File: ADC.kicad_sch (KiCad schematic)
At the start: 83 parts, among them J1 Conn_01x03_Pin, J2 Screw_Terminal_01x02, J3 Screw_Terminal_01x08, SW1 SW_SPDT, U1 ADS1256IDBR, U12 ADR421ARMZ, U2 MCU-STM32F407VET6_LQFP100_, U3 ADM2483xRW, U4 LM2596S-5, U5 DCP010505BP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

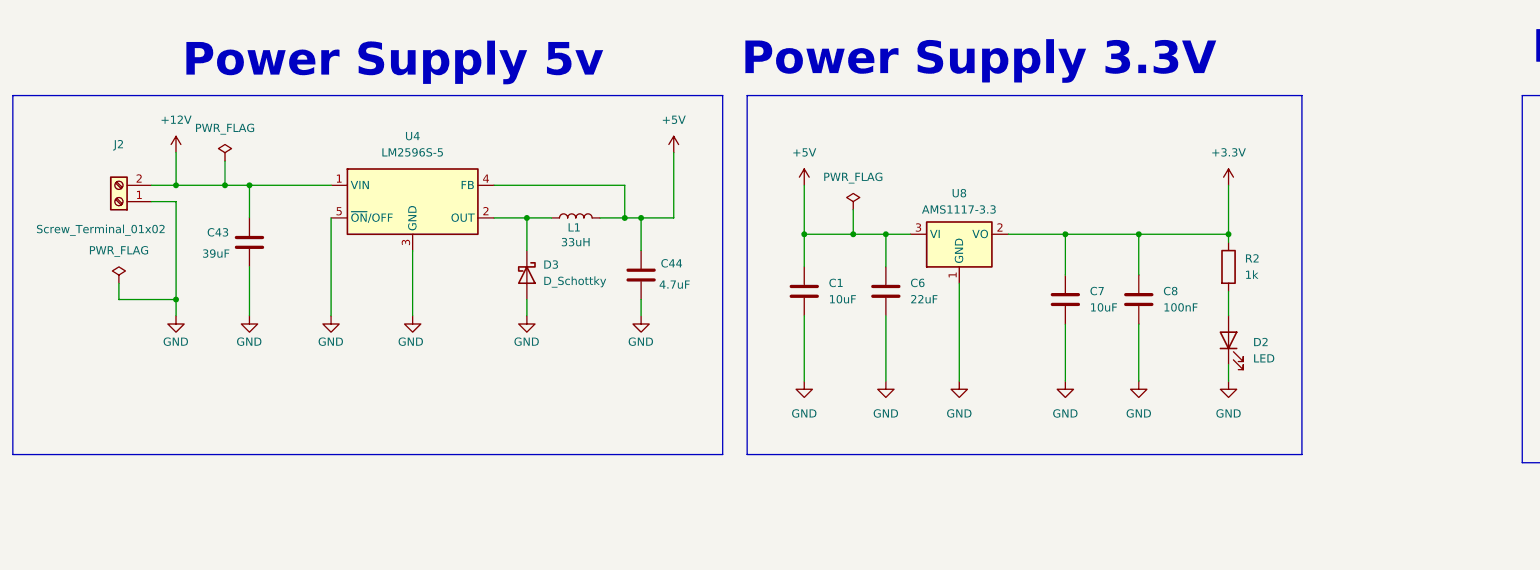
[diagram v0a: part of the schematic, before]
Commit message: Sửa tụ
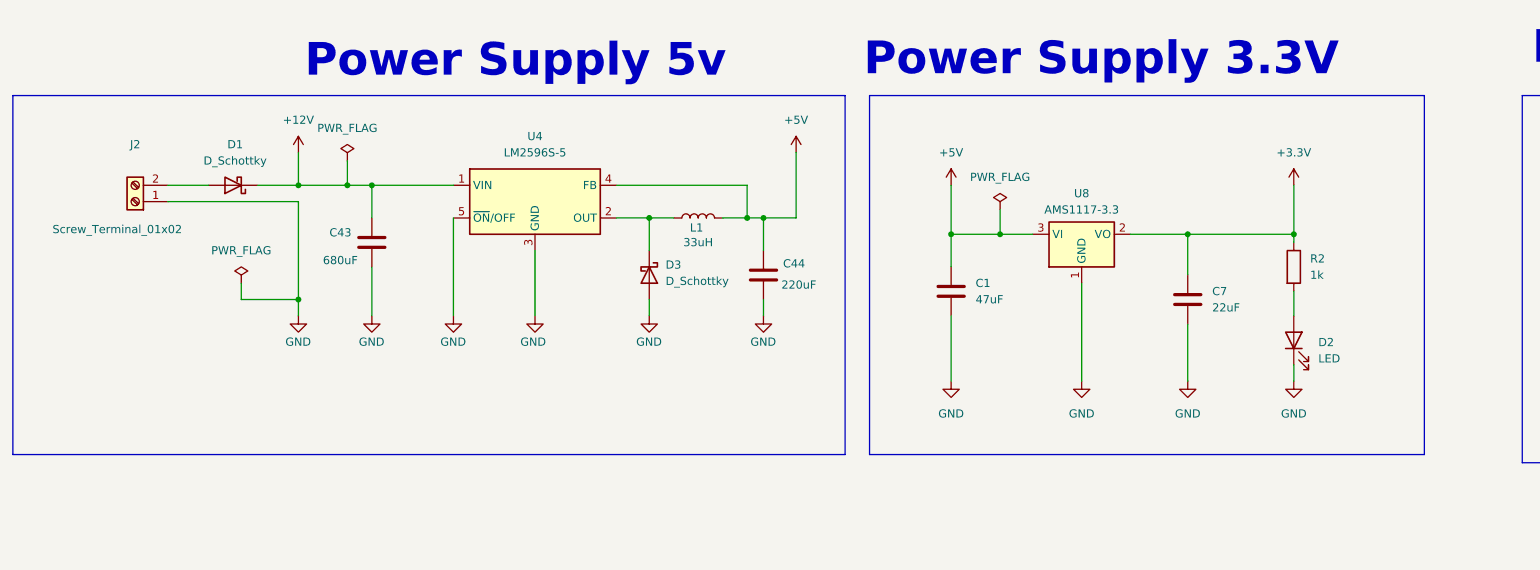
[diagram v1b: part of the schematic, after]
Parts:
- removed C6: 22uF, symbol Device:C
- removed C8: 100nF, symbol Device:C
- added D1: D_Schottky, symbol Device:D_Schottky
- C1: value 10uF -> 47uF
- C43: value 39uF -> 680uF
- C44: value 4.7uF -> 220uF
- C7: value 10uF -> 22uF
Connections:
- net +12V: now also D1.1 (K); no longer J2.2 (Pin_2)
- new net: D1.2 (A), J2.2 (Pin_2)
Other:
- moved on the sheet: C1, C43, C44, C7, D2, D3, J2, L1, R2, U4, U8

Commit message: Bảo vệ nguồn
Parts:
- added F1: Polyfuse, symbol Device:Polyfuse
- added RV2: Varistor, symbol Device:Varistor
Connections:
- net +12V: now also J2.2 (Pin_2), F1.1; no longer C43.1, D1.1 (K), U4.1 (VIN)
- net GND: now also D1.2 (A), RV2.2
- new net: C43.1, D1.1 (K), F1.2, RV2.1, U4.1 (VIN)
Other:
- moved on the sheet: C1, C43, C44, C7, C9, D2, D3, L1, R2, U4, U5, U8

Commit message: ...
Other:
- moved on the sheet: C1, C12, C13, C14, C15, C16, C17, C18, C19, C20, C21, C22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

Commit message: Thêm GND
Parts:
- removed J3: Screw_Terminal_01x08, symbol Connector:Screw_Terminal_01x08
- added J3: Screw_Terminal_01x09, symbol Connector:Screw_Terminal_01x09
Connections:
- net GND: now also J3.9 (Pin_9)
- net VinN1: now also J3.2 (Pin_2)
- net VinN2: now also J3.4 (Pin_4)
- net VinN3: now also J3.6 (Pin_6)
- net VinN4: now also J3.8 (Pin_8)
- net VinP1: now also J3.1 (Pin_1)
- net VinP2: now also J3.3 (Pin_3)
- net VinP3: now also J3.5 (Pin_5)
- net VinP4: now also J3.7 (Pin_7)
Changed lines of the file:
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@@
 	(wire
 		(pts
+			(xy 350.52 424.18) (xy 349.25 424.18)
+		)
+		(stroke
+			(width 0)
+			(type default)
+		)
+	)
+	(wire
+		(pts
 			(xy 652.78 427.99) (xy 652.78 425.45)
 		)
@@
 	(wire
 		(pts
+			(xy 349.25 424.18) (xy 349.25 427.99)
+		)
+		(stroke
+			(width 0)
+			(type default)
+		)
+	)
+	(wire
+		(pts
 			(xy 510.54 365.76) (xy 515.62 365.76)
 		)
@@
 	)
 	(rectangle
-		(start 302.26 340.36)
-		(end 525.78 500.38)
+		(start 300.99 341.63)
+		(end 558.8 501.65)
 		(stroke
 			(width 0)
@@
 	)
 	(symbol
+		(lib_id "Connector:Screw_Terminal_01x09")
+		(at 355.6 414.02 0)
+		(unit 1)
+		(exclude_from_sim no)
+		(in_bom yes)
+		(on_board yes)
+		(dnp no)
+		(fields_autoplaced yes)
+		(property "Reference" "J3"
+			(at 358.14 412.7499 0)
+			(effects
+				(font
+					(size 1.27 1.27)
+				)
+				(justify left)
+			)
+		)
+		(property "Value" "Screw_Terminal_01x09"
+			(at 358.14 415.2899 0)
+			(effects
+				(font
+					(size 1.27 1.27)
+				)
+				(justify left)
+			)
+		)
+		(property "Footprint" ""
+			(at 355.6 414.02 0)
+			(effects
+				(font
+					(size 1.27 1.27)
+				)
+				(hide yes)
+			)
+		)
+		(property "Datasheet" "~"
+			(at 355.6 414.02 0)
+			(effects
+				(font
+					(size 1.27 1.27)
+				)
+				(hide yes)
+			)
+		)
+		(property "Description" "Generic screw terminal, single row, 01x09, script generated (kicad-library-utils/schlib/autogen/connector/)"
+			(at 355.6 414.02 0)
+			(effects
+				(font
+					(size 1.27 1.27)
+				)
+				(hide yes)
+			)
+		)
+		(pin "8"
+		)
+		(pin "7"
+		)
+		(pin "2"
+		)
+		(pin "3"
+		)
+		(pin "6"
+		)
+		(pin "9"
+		)
+		(pin "1"
+		)
+		(pin "4"
+		)
+		(pin "5"
+		)
+		(instances
+			(project ""
+				(path "/c7ceee6a-ba62-44b0-b5ba-f64f163625fc"
+					(reference "J3")
+					(unit 1)
+				)
+			)
+		)
+	)
+	(symbol
 		(lib_id "Device:C")
 		(at 651.51 408.94 0)
@@
 	)
 	(symbol
+		(lib_id "power:GND")
+		(at 349.25 427.99 0)
+		(unit 1)
+		(exclude_from_sim no)
+		(in_bom yes)
+		(on_board yes)
+		(dnp no)
+		(property "Reference" "#PWR058"
+			(at 349.25 434.34 0)
+			(effects
+				(font
+					(size 1.27 1.27)
+				)
+				(hide yes)
+			)
+		)
+		(property "Value" "GND"
+			(at 347.472 432.308 0)
+			(effects
+				(font
+					(size 1.27 1.27)
+				)
+				(justify left)
+			)
+		)
+		(property "Footprint" ""
+			(at 349.25 427.99 0)
+			(effects
+				(font
+					(size 1.27 1.27)
+				)
+				(hide yes)
+			)
+		)
+		(property "Datasheet" ""
+			(at 349.25 427.99 0)
+			(effects
+				(font
+					(size 1.27 1.27)
+				)
+				(hide yes)
+			)
+		)
+		(property "Description" "Power symbol creates a global label with name \"GND\" , ground"
+			(at 349.25 427.99 0)
+			(effects
+				(font
+					(size 1.27 1.27)
+				)
+				(hide yes)
+			)
+		)
+		(pin "1"
+		)
+		(instances
+			(project "ADC"
+				(path "/c7ceee6a-ba62-44b0-b5ba-f64f163625fc"
+					(reference "#PWR058")
+					(unit 1)
+				)
+			)
+		)
+	)
+	(symbol
 		(lib_id "power:PWR_FLAG")
 		(at 347.98 355.6 0)
@@
 					(unit 1)
 				)
-			)
-		)
-	)
-	(symbol
-		(lib_id "Connector:Screw_Terminal_01x08")
-		(at 355.6 411.48 0)
-		(unit 1)
-		(exclude_from_sim no)
-		(in_bom yes)
-		(on_board yes)
-		(dnp no)
-		(fields_autoplaced yes)
-		(property "Reference" "J3"
-			(at 358.14 411.4799 0)
-			(effects
-				(font
-					(size 1.27 1.27)
-				)
-				(justify left)
-			)
-		)
-		(property "Value" "Screw_Terminal_01x08"
-			(at 358.14 414.0199 0)
-			(effects
-				(font
-					(size 1.27 1.27)
-				)
-				(justify left)
-			)
-		)
-		(property "Footprint" ""
-			(at 355.6 411.48 0)
-			(effects
-				(font
-					(size 1.27 1.27)
-				)
-				(hide yes)
-			)
-		)
-		(property "Datasheet" "~"
-			(at 355.6 411.48 0)
-			(effects
-				(font
-					(size 1.27 1.27)
-				)
-				(hide yes)
-			)
-		)
-		(property "Description" "Generic screw terminal, single row, 01x08, script generated (kicad-library-utils/schlib/autogen/connector/)"
-			(at 355.6 411.48 0)
-			(effects
-				(font
-					(size 1.27 1.27)
-				)
-				(hide yes)
-			)
-		)
-		(pin "3"
-		)
-		(pin "6"
-		)
-		(pin "4"
-		)
-		(pin "1"
-		)
-		(pin "8"
-		)
-		(pin "7"
-		)
-		(pin "5"
-		)
-		(pin "2"
-		)
-		(instances
-			(project ""
-				(path "/c7ceee6a-ba62-44b0-b5ba-f64f163625fc"
-					(reference "J3")
-					(unit 1)
-				)

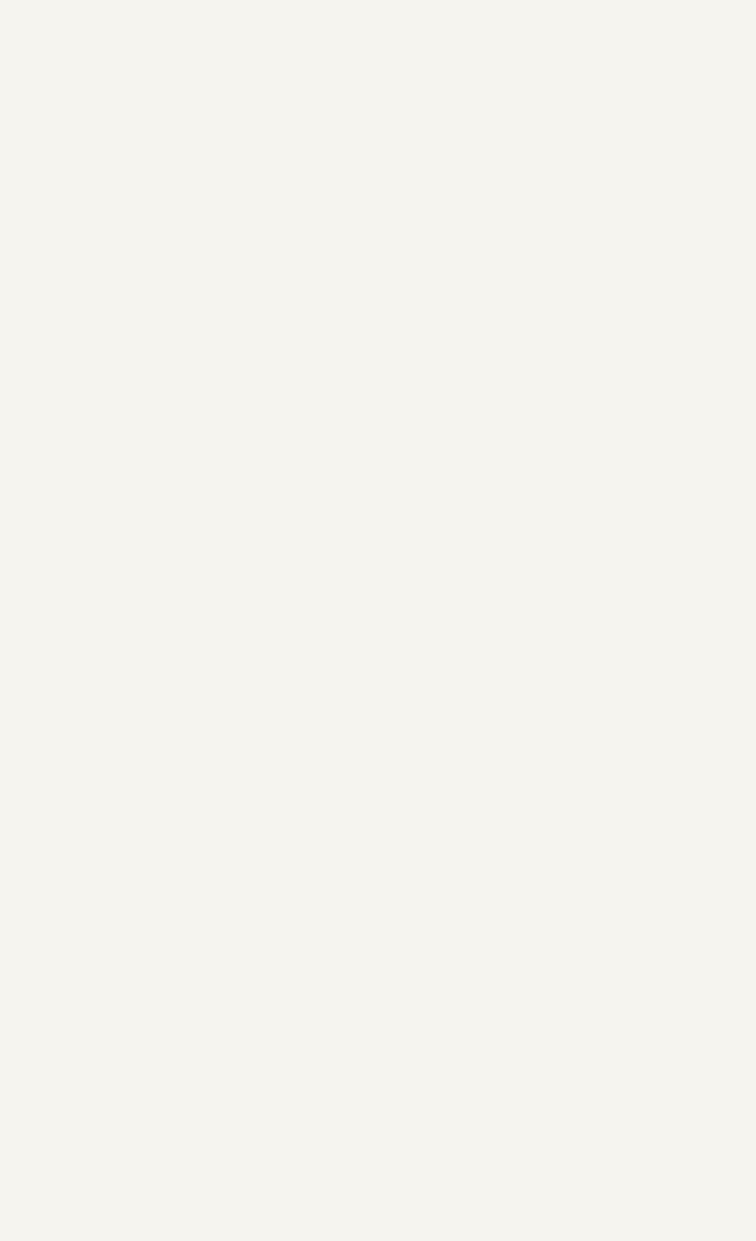
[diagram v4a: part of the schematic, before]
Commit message: Thêm linh kiện
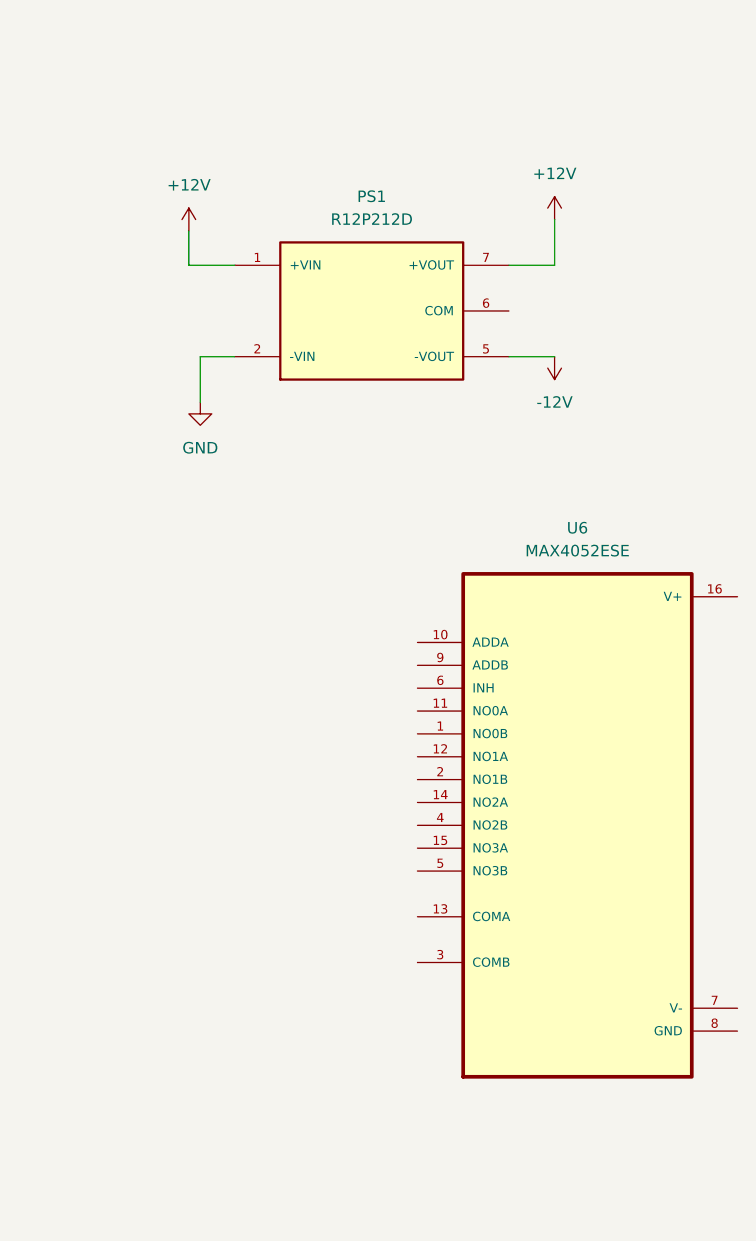
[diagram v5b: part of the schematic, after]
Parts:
- added PS1: R12P212D, R12P212D:CONV_R12P212D, symbol R12P212D:R12P212D
- added U6: MAX4052ESE, MAX4052ESE:SOIC127P600X175-16N, symbol MAX4052ESE:MAX4052ESE
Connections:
- net +12V: now also PS1.1 (+VIN), PS1.7 (+VOUT)
- net GND: now also PS1.2 (-VIN)
- new net -12V: PS1.5 (-VOUT)

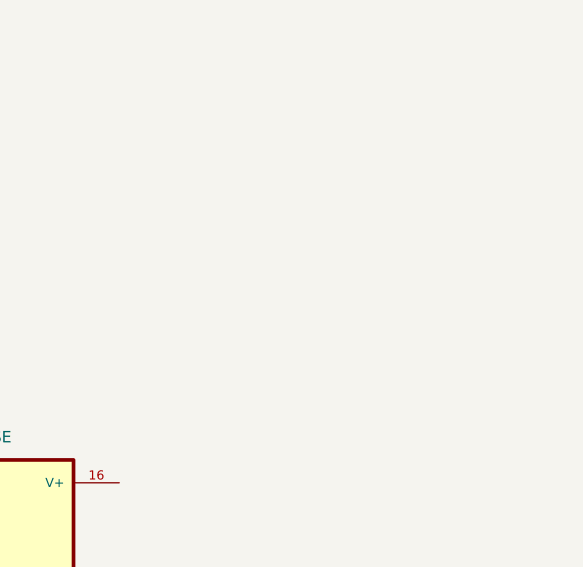
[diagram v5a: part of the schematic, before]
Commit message: Thêm 3 linh kiện
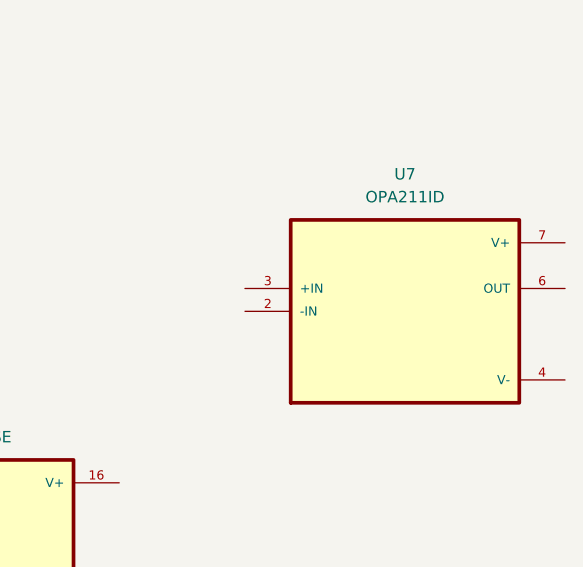
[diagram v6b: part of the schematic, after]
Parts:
- added U7: OPA211ID, OPA211ID:SOIC127P599X175-8N, symbol OPA211ID:OPA211ID
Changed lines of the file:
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@@
+	)
+	(symbol
+		(lib_id "OPA211ID:OPA211ID")
+		(at 924.56 410.21 0)
+		(unit 1)
+		(exclude_from_sim no)
+		(in_bom yes)
+		(on_board yes)
+		(dnp no)
+		(fields_autoplaced yes)
+		(property "Reference" "U7"
+			(at 924.56 394.97 0)
+			(effects
+				(font
+					(size 1.27 1.27)
+				)
+			)
+		)
+		(property "Value" "OPA211ID"
+			(at 924.56 397.51 0)
+			(effects
+				(font
+					(size 1.27 1.27)
+				)
+			)
+		)
+		(property "Footprint" "OPA211ID:SOIC127P599X175-8N"
+			(at 924.56 410.21 0)
+			(effects
+				(font
+					(size 1.27 1.27)
+				)
+				(justify bottom)
+				(hide yes)
+			)
+		)
+		(property "Datasheet" ""
+			(at 924.56 410.21 0)
+			(effects
+				(font
+					(size 1.27 1.27)
+				)
+				(hide yes)
+			)
+		)
+		(property "Description" ""
+			(at 924.56 410.21 0)
+			(effects
+				(font
+					(size 1.27 1.27)
+				)
+				(hide yes)
+			)
+		)
+		(property "MF" "Texas Instruments"
+			(at 924.56 410.21 0)
+			(effects
+				(font
+					(size 1.27 1.27)
+				)
+				(justify bottom)
+				(hide yes)
+			)
+		)
+		(property "Description_1" "\n                        \n                            1.1nV/rtHz Noise, Low-Power, Precision Operational Amplifier\n                        \n"
+			(at 924.56 410.21 0)
+			(effects
+				(font
+					(size 1.27 1.27)
+				)
+				(justify bottom)
+				(hide yes)
+			)
+		)
+		(property "Package" "SOIC-8 Texas Instruments"
+			(at 924.56 410.21 0)
+			(effects
+				(font
+					(size 1.27 1.27)
+				)
+				(justify bottom)
+				(hide yes)
+			)
+		)
+		(property "Price" "None"
+			(at 924.56 410.21 0)
+			(effects
+				(font
+					(size 1.27 1.27)
+				)
+				(justify bottom)
+				(hide yes)
+			)
+		)
+		(property "SnapEDA_Link" "https://www.snapeda.com/parts/OPA211ID/Texas+Instruments/view-part/?ref=snap"
+			(at 924.56 410.21 0)
+			(effects
+				(font
+					(size 1.27 1.27)
+				)
+				(justify bottom)
+				(hide yes)
+			)
+		)
+		(property "MP" "OPA211ID"
+			(at 924.56 410.21 0)
+			(effects
+				(font
+					(size 1.27 1.27)
+				)
+				(justify bottom)
+				(hide yes)
+			)
+		)
+		(property "Availability" "In Stock"
+			(at 924.56 410.21 0)
+			(effects
+				(font
+					(size 1.27 1.27)
+				)
+				(justify bottom)
+				(hide yes)
+			)
+		)
+		(property "Check_prices" "https://www.snapeda.com/parts/OPA211ID/Texas+Instruments/view-part/?ref=eda"
+			(at 924.56 410.21 0)
+			(effects
+				(font
+					(size 1.27 1.27)
+				)
+				(justify bottom)
+				(hide yes)
+			)
+		)
+		(pin "2"
+		)
+		(pin "6"
+		)
+		(pin "3"
+		)
+		(pin "7"
+		)
+		(pin "4"
+		)
+		(instances
+			(project ""
+				(path "/c7ceee6a-ba62-44b0-b5ba-f64f163625fc"
+					(reference "U7")
+					(unit 1)
+				)
+			)
+		)
 	)
 	(symbol

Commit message: ADD ADG
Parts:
- removed RV2: Varistor, symbol Device:Varistor
- added D6: D_TVS_Filled, symbol Device:D_TVS_Filled
- added L2: 100uH, symbol Device:L
- added U9: ADG5412FBCPZ-RL7, ADG5412FBCPZ-RL7:QFN65P400X400X80-17N, symbol ADG5412FBCPZ-RL7:ADG5412FBCPZ-RL7
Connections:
- net +12V: now also U4.1 (VIN); no longer F1.1, J2.2 (Pin_2), PS1.1 (+VIN)
- net GND: now also PS1.6 (COM), D6.1 (A1)
- net at D1.1 (K), F1.2: now also D6.2 (A2), L2.1; no longer C43.1, U4.1 (VIN)
- new net: C43.1, L2.2, PS1.1 (+VIN)
- new net +12V_IN: F1.1, J2.2 (Pin_2)
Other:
- moved on the sheet: C43, C44, D3, F1, J2, L1, PS1, U4, U6, U7

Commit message: Add digital
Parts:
- added C2, C3: 100nF, Capacitor_SMD:C_0402_1005Metric, symbol Device:C
- added U10: CD4514BM, CD4514BM:SOIC127P1030X265-24N, symbol CD4514BM:CD4514BM
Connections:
- net +12V: now also C2.1; no longer U4.1 (VIN)
- net -12V: now also C3.1
- net GND: now also C2.2, C3.2
- net at C43.1, L2.2, PS1.1 (+VIN): now also U4.1 (VIN)
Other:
- moved on the sheet: C43, C44, D1, D3, D6, F1, J2, L1, L2, PS1, U4
